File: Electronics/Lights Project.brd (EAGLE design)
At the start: 71.1 x 54.3 mm, 16 parts

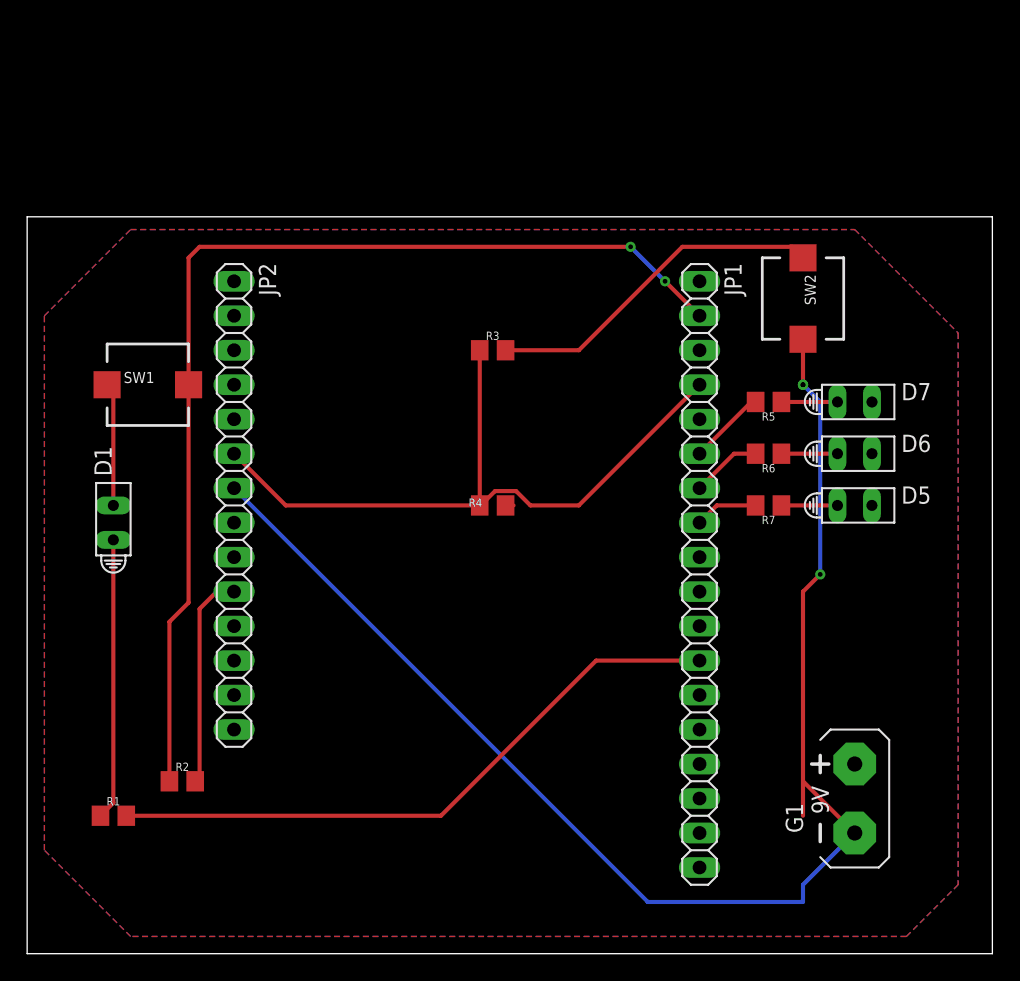
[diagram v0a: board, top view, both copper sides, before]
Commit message: Updated PCB and Schematic: added headers and holes
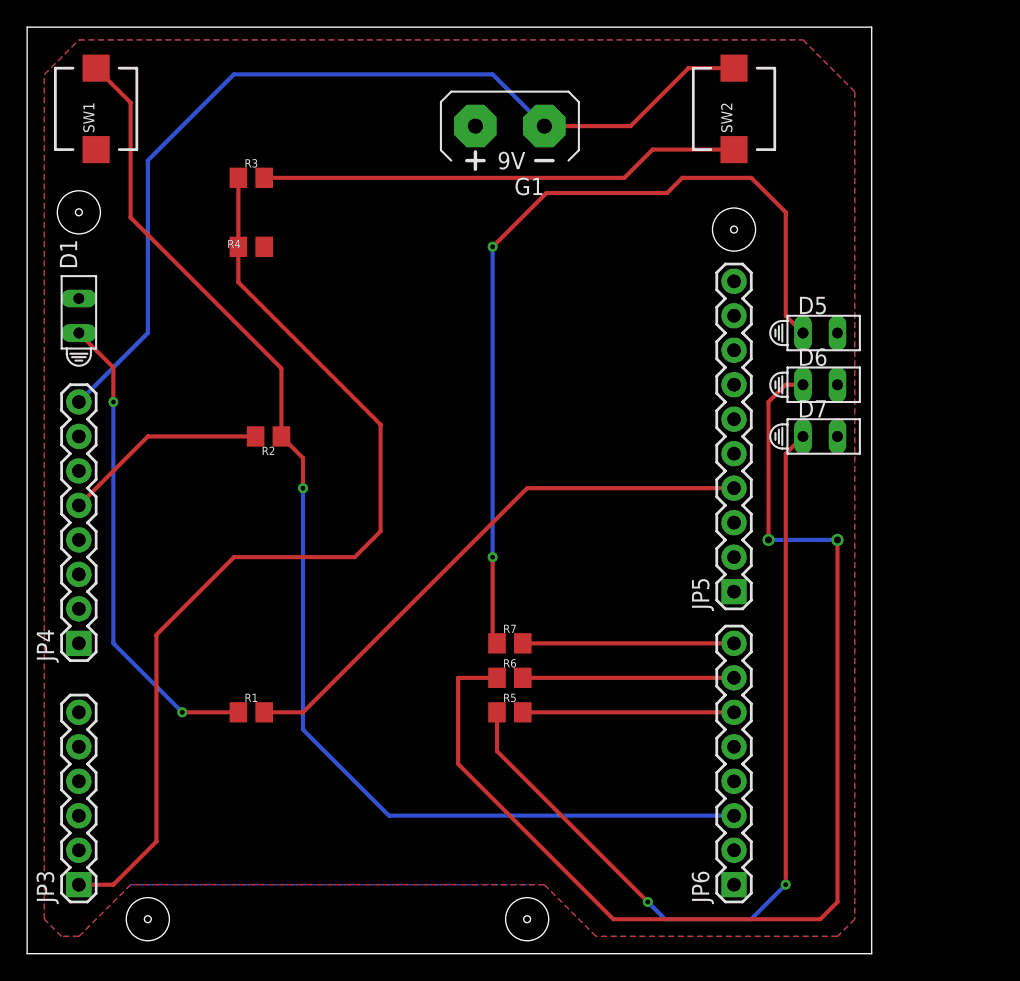
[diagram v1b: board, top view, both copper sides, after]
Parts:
- removed JP1: (no value), adafruit:1X18
- removed JP2: (no value), adafruit:1X14
- added JP3: (no value), arduino_jw:CONN-1X06
- added JP4, JP6: (no value), arduino_jw:CONN-1X08
- added JP5: ARDUINO_CONN-IO_HSIP, arduino_jw:CONN-1X10
- moved G1 55.7 mm to (35.6, 61.0), turned to 90 degrees
- moved R5 29.8 mm to (35.6, 17.8), turned to 0 degrees
- moved R2 26.2 mm to (17.8, 38.1), turned to 180 degrees
- moved R4 26.1 mm to (16.5, 52.1)
- moved R6 25.2 mm to (35.6, 20.3), turned to 0 degrees
- moved R3 21.8 mm to (16.5, 57.1)
- moved R7 21.6 mm to (35.6, 22.9), turned to 0 degrees
- moved SW1 20.7 mm to (5.08, 62.2), turned to 90 degrees
- moved D1 15.5 mm to (3.81, 47.0)
- moved SW2 14.9 mm to (52.1, 62.2), turned to 90 degrees
- moved D5 13.0 mm to (58.4, 45.7)
- moved R1 12.7 mm to (16.5, 17.8)
- moved D6 5.68 mm to (58.4, 41.9)
- moved D7 3.59 mm to (58.4, 38.1)
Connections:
- net GND: now also JP5.7; no longer JP1.15
- net N$1: now also JP4.8; no longer JP2.7
- net N$10: now also JP6.7; no longer JP1.7
- net N$11: now also JP6.8; no longer JP1.8
- net N$13: now also JP3.1; no longer JP1.4, JP2.6
- net N$14: now also JP4.5; no longer JP2.10
- net N$2: now also JP5.4; no longer JP1.12
- net N$5: now also JP6.3; no longer JP1.2
- net N$8: now also JP6.6; no longer JP1.6
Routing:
- net N$7: track 4.13 -> 87.4 mm, vias 0 -> 2
- net N$9: track 4.13 -> 63.9 mm, vias 0 -> 2
- net N$4: track 4.13 -> 63.5 mm, vias 0 -> 2
- net N$1: track 102.7 -> 69.0 mm, vias 3 -> 0
- net N$13: track 51.9 -> 72.3 mm
- net N$3: track 20.7 -> 35.7 mm, vias 0 -> 2
- net N$11: track 4.66 -> 15.6 mm
- net N$10: track 5.18 -> 15.6 mm
- net N$6: track 25.4 -> 35.5 mm
- net N$5: track 79.5 -> 89.4 mm, vias 2 -> 1
- net N$8: track 5.71 -> 15.6 mm
- net GND: track 9.67 -> 0.00 mm
- net N$2: track 47.0 -> 41.4 mm
- net N$14: track 15.9 -> 15.1 mm
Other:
- board size 71.1 x 54.3 mm -> 62.2 x 68.2 mm
